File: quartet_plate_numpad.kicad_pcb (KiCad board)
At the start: 2 copper layers, 82.2 x 100 mm, 7 parts

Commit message: Get ready for JLCPCB
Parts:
- moved H2 92.4 mm to (3.81, 3.81)
- moved H4 92.4 mm to (3.81, 96.2)
- moved H6 34.1 mm to (51.0, 41.0)
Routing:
- added copper zone on B.Cu, net (none)
- added copper zone on F.Cu, net (none)
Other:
- board text added: "JLCJLCJLCJLC"
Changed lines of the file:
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@@
   (general
     (thickness 1.6)
-    (drawings 8)
+    (drawings 9)
     (tracks 0)
     (zones 0)
@@
       (outputformat 1)
       (mirror false)
-      (drillshape 1)
+      (drillshape 0)
       (scaleselection 1)
-      (outputdirectory ""))
+      (outputdirectory "export_plate_numpad/"))
   )
   (net 0 "")
@@
     (at 12.525 12.525)
     (descr "Keyboard cutout for a standard numpad")
-    (fp_text reference H7 (at 0 -9.525) (layer F.SilkS)
+    (fp_text reference H7 (at 0 -9.525) (layer F.SilkS) hide
       (effects (font (size 1 1) (thickness 0.15)))
     )
@@
   )
   (module Gigahawk:DOT (layer F.Cu)
-    (at 85.09 39.37)
+    (at 51 41)
     (fp_text reference H6 (at 0.635 -1.905) (layer F.Fab)
       (effects (font (size 1 1) (thickness 0.15)))
@@
     (tags "mounting hole 2.2mm m2")
     (attr virtual)
-    (fp_text reference H5 (at 0 -3.2) (layer F.SilkS)
+    (fp_text reference H5 (at 0 -3.2) (layer F.SilkS) hide
       (effects (font (size 1 1) (thickness 0.15)))
     )
     (fp_text value "Center(51,41)" (at 0 3.2) (layer F.Fab)
-      (effects (font (size 1 1) (thickness 0.15)))
-    )
-    (fp_circle (center 0 0) (end 2.45 0) (layer F.CrtYd) (width 0.05))
-    (fp_circle (center 0 0) (end 2.2 0) (layer Cmts.User) (width 0.15))
-    (fp_text user %R (at 0.3 0) (layer F.Fab)
-      (effects (font (size 1 1) (thickness 0.15)))
-    )
-    (pad 1 thru_hole circle (at 0 0) (size 4.4 4.4) (drill 2.2) (layers *.Cu *.Mask))
-  )
-  (module MountingHole:MountingHole_2.2mm_M2_Pad (layer F.Cu)
-    (at 96.19 96.19)
-    (descr "Mounting Hole 2.2mm, M2")
-    (tags "mounting hole 2.2mm m2")
-    (attr virtual)
-    (fp_text reference H4 (at 0 -3.2) (layer F.SilkS)
-      (effects (font (size 1 1) (thickness 0.15)))
-    )
-    (fp_text value "BottomRight(96.19,96.19)" (at 0 3.2) (layer F.Fab)
       (effects (font (size 1 1) (thickness 0.15)))
     )
@@
     (tags "mounting hole 2.2mm m2")
     (attr virtual)
-    (fp_text reference H3 (at 0 -3.2) (layer F.SilkS)
-      (effects (font (size 1 1) (thickness 0.15)))
-    )
-    (fp_text value "BottomLeft(3.81,96.19)" (at 0 3.2) (layer F.Fab)
+    (fp_text reference H4 (at 0 -3.2) (layer F.SilkS) hide
+      (effects (font (size 1 1) (thickness 0.15)))
+    )
+    (fp_text value "BottomRight(96.19,96.19)" (at 0 3.2) (layer F.Fab)
       (effects (font (size 1 1) (thickness 0.15)))
     )
@@
   )
   (module MountingHole:MountingHole_2.2mm_M2_Pad (layer F.Cu)
-    (at 96.19 3.81)
+    (at 3.81 96.19)
     (descr "Mounting Hole 2.2mm, M2")
     (tags "mounting hole 2.2mm m2")
     (attr virtual)
-    (fp_text reference H2 (at 0 -3.2) (layer F.SilkS)
-      (effects (font (size 1 1) (thickness 0.15)))
-    )
-    (fp_text value "TopRight(96.19,3.81)" (at 0 3.2) (layer F.Fab)
+    (fp_text reference H3 (at 0 -3.2) (layer F.SilkS) hide
+      (effects (font (size 1 1) (thickness 0.15)))
+    )
+    (fp_text value "BottomLeft(3.81,96.19)" (at 0 3.2) (layer F.Fab)
       (effects (font (size 1 1) (thickness 0.15)))
     )
@@
     (tags "mounting hole 2.2mm m2")
     (attr virtual)
-    (fp_text reference H1 (at 0 -3.2) (layer F.SilkS)
-      (effects (font (size 1 1) (thickness 0.15)))
-    )
-    (fp_text value "TopLeft(3.81,3.81)" (at 0 3.2) (layer F.Fab)
+    (fp_text reference H2 (at 0 -3.2) (layer F.SilkS) hide
+      (effects (font (size 1 1) (thickness 0.15)))
+    )
+    (fp_text value "TopRight(96.19,3.81)" (at 0 3.2) (layer F.Fab)
       (effects (font (size 1 1) (thickness 0.15)))
     )
@@
     )
     (pad 1 thru_hole circle (at 0 0) (size 4.4 4.4) (drill 2.2) (layers *.Cu *.Mask))
+  )
+  (module MountingHole:MountingHole_2.2mm_M2_Pad (layer F.Cu)
+    (at 3.81 3.81)
+    (descr "Mounting Hole 2.2mm, M2")
+    (tags "mounting hole 2.2mm m2")
+    (attr virtual)
+    (fp_text reference H1 (at 0 -3.2) (layer F.SilkS) hide
+      (effects (font (size 1 1) (thickness 0.15)))
+    )
+    (fp_text value "TopLeft(3.81,3.81)" (at 0 3.2) (layer F.Fab)
+      (effects (font (size 1 1) (thickness 0.15)))
+    )
+    (fp_circle (center 0 0) (end 2.45 0) (layer F.CrtYd) (width 0.05))
+    (fp_circle (center 0 0) (end 2.2 0) (layer Cmts.User) (width 0.15))
+    (fp_text user %R (at 0.3 0) (layer F.Fab)
+      (effects (font (size 1 1) (thickness 0.15)))
+    )
+    (pad 1 thru_hole circle (at 0 0) (size 4.4 4.4) (drill 2.2) (layers *.Cu *.Mask))
+  )
+  (gr_text JLCJLCJLCJLC (at 61.976 78.74 90) (layer B.SilkS)
+    (effects (font (size 0.8 0.8) (thickness 0.15)) (justify mirror))
   )
   (gr_line (start 3.81 0) (end 78.4 0) (angle 90) (layer Edge.Cuts) (width 0.05))
@@
   (gr_arc (start 78.4 96.19) (end 78.4 100) (angle -90) (layer Edge.Cuts) (width 0.05))
   (gr_arc (start 78.4 3.81) (end 82.21 3.81) (angle -90) (layer Edge.Cuts) (width 0.05))
+  (zone (net 0) (net_name "") (layer F.Cu) (hatch edge 0.508)
+    (connect_pads (clearance 0.508))
+    (min_thickness 0.254)
+    (fill yes (arc_segments 32) (thermal_gap 0.508) (thermal_bridge_width 0.508))
+    (polygon
+      (pts
+        (xy 83.82 101.6) (xy -2.54 101.6) (xy -2.54 -2.54) (xy 83.82 -2.54)
+      )
+    )
+  )
+  (zone (net 0) (net_name "") (layer B.Cu) (hatch edge 0.508)
+    (connect_pads (clearance 0.508))
+    (min_thickness 0.254)
+    (fill yes (arc_segments 32) (thermal_gap 0.508) (thermal_bridge_width 0.508))
+    (polygon
+      (pts
+        (xy 83.82 101.6) (xy -2.54 101.6) (xy -2.54 -2.54) (xy 83.82 -2.54)
+      )
+    )
+  )
 )

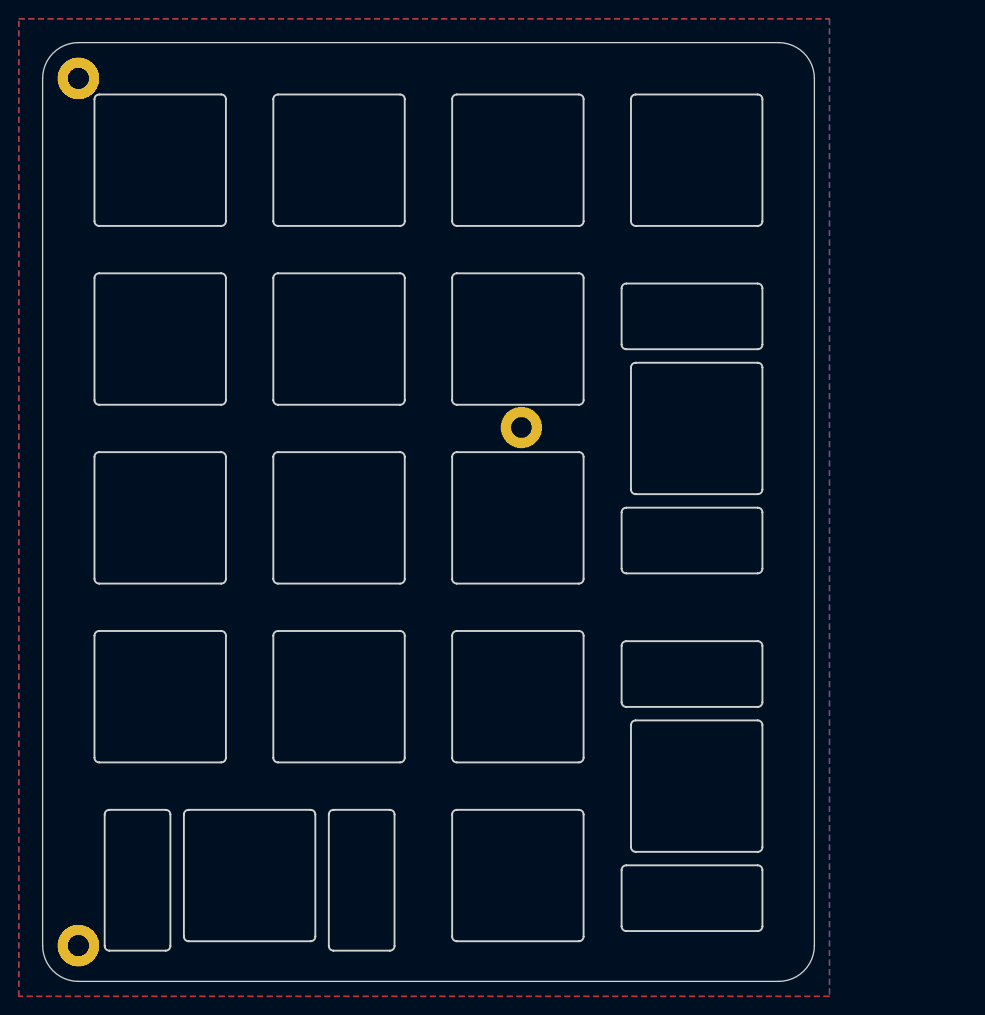
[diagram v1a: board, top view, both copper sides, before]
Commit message: Remove soldermask and copper fill
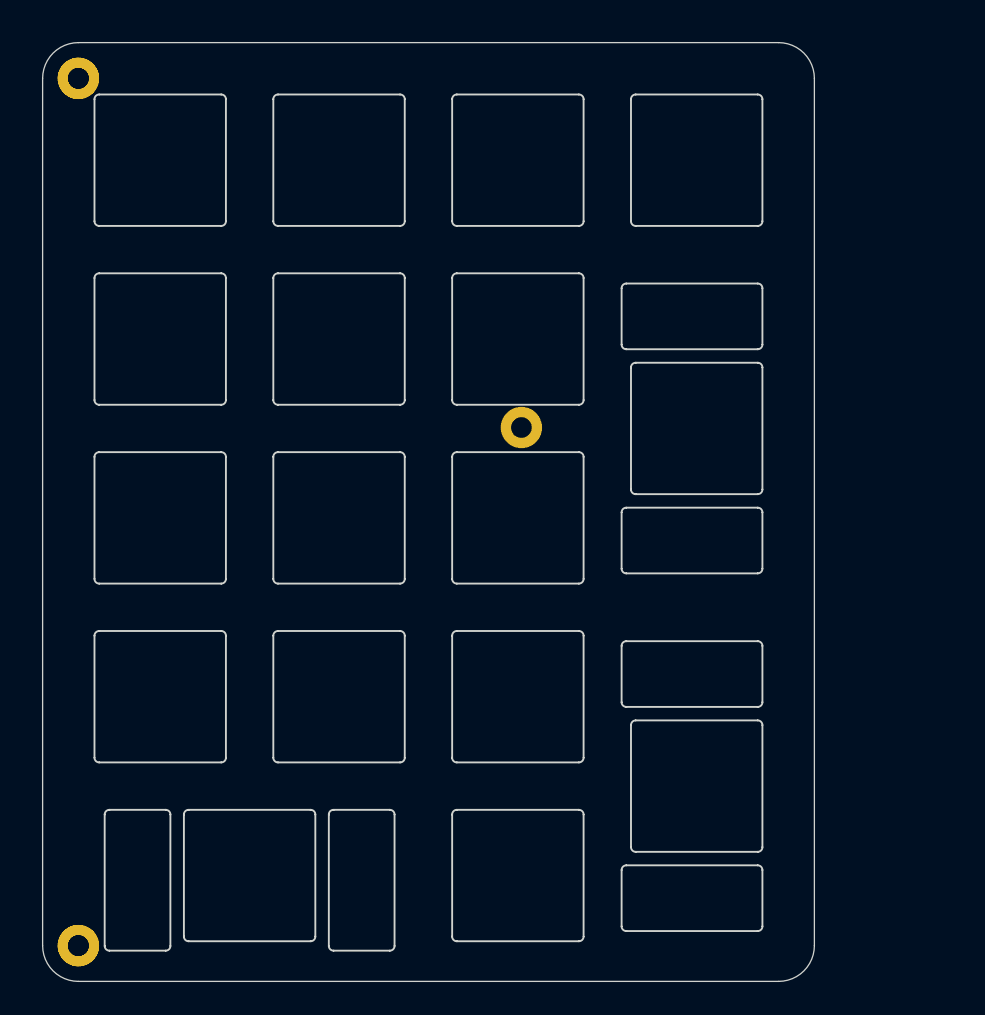
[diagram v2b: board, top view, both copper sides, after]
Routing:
- removed copper zone on B.Cu, net (none)
- removed copper zone on F.Cu, net (none)
